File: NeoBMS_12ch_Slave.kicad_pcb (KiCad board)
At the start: 2 copper layers, 60 x 60 mm, 73 parts, among them IC1 LTC6804-2, P1 Low Cells, P2 High Cells, P3 BUS, P4 Expansion, Q1 Q_NPN_BCEC, SW1 Address, T1 CM Choke, T2 TRANSFORMER

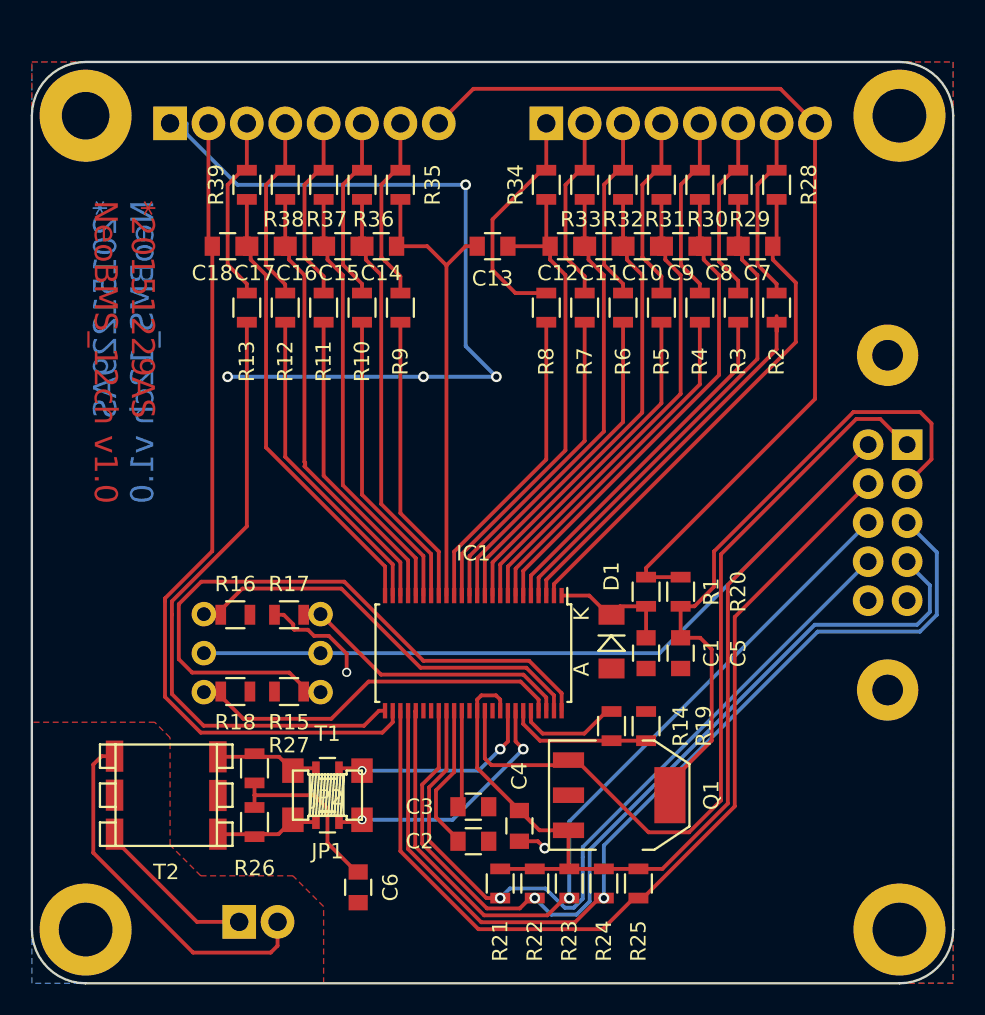
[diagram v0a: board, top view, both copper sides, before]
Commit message: - integrated balancer and filter resistors into one - changed filter/balancer resistors to 1206 - changed BIAS network to 1k5 + 470R - relocated BIAS network
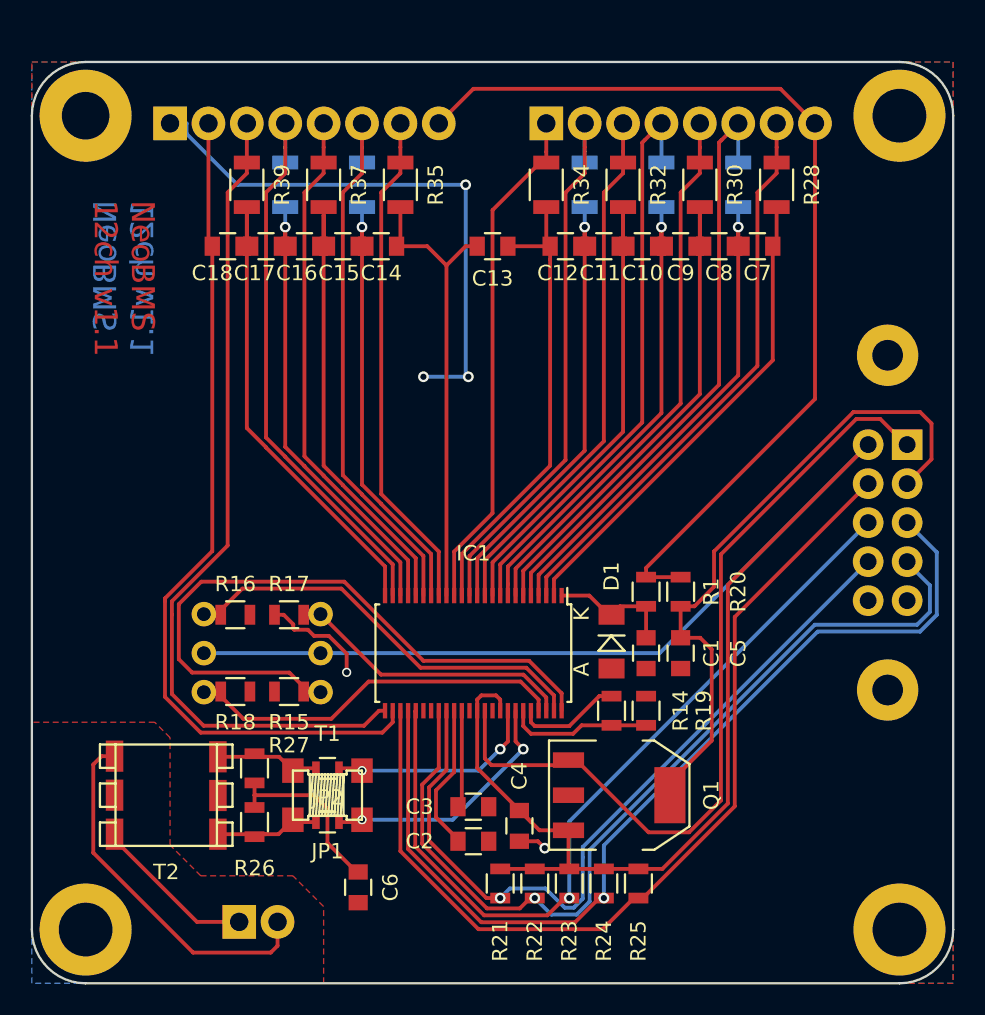
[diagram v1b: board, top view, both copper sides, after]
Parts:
- removed R10, R11, R12, R13, R2, R3, R4, R5, R6, R7, R8, R9: 100, Resistors_SMD:R_0805
- R14: value 2k7 -> 1k5
- R19: value 1k2 -> 470
- R28, R30, R32, R34, R35, R37, R39: footprint Resistors_SMD:R_0805 -> Resistors_SMD:R_1206
- R29, R31, R33, R36, R38: footprint Resistors_SMD:R_0805 -> Resistors_SMD:R_1206; moved to B.Cu
- T2: value TRANSFORMER -> PE-68386N
- moved R14 1.00 mm to (74.8, 66.2)
- moved R19 1.00 mm to (77.0, 66.2)
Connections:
- IC1 pad 11: Net-(IC1-Pad11) -> /Cell_8+
- IC1 pad 13: Net-(IC1-Pad13) -> /Cell_7+
- IC1 pad 15: Net-(IC1-Pad15) -> /Cell_6+
- IC1 pad 17: Net-(IC1-Pad17) -> /Cell_5+
- IC1 pad 19: Net-(IC1-Pad19) -> /Cell_4+
- IC1 pad 21: Net-(IC1-Pad21) -> /Cell_3+
- IC1 pad 23: Net-(IC1-Pad23) -> /Cell_2+
- IC1 pad 25: Net-(IC1-Pad25) -> /Cell_1+
- IC1 pad 3: Net-(IC1-Pad3) -> /Cell_12+
- IC1 pad 39: (no net) -> Net-(IC1-Pad39)
- IC1 pad 5: Net-(IC1-Pad5) -> /Cell_11+
- IC1 pad 7: Net-(IC1-Pad7) -> /Cell_10+
- IC1 pad 9: Net-(IC1-Pad9) -> /Cell_9+
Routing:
- net /Cell_1+: track 12.6 -> 54.3 mm
- net Net-(IC1-Pad25): track 41.4 -> 0.00 mm
- net /Cell_11+: track 12.6 -> 38.9 mm
- net /Cell_9+: track 12.6 -> 37.6 mm
- net Net-(IC1-Pad3): track 25.0 -> 0.00 mm
- net /Cell_2+: track 12.6 -> 37.2 mm
- net /Cell_12+: track 12.9 -> 37.0 mm
- net /Cell_7+: track 12.6 -> 36.4 mm
- net /Cell_4+: track 12.5 -> 36.0 mm
- net Net-(IC1-Pad5): track 23.4 -> 0.00 mm
- net /Cell_10+: track 12.6 -> 35.7 mm
- net Net-(IC1-Pad7): track 22.8 -> 0.00 mm
- net Net-(IC1-Pad9): track 22.1 -> 0.00 mm
- net /Cell_8+: track 12.5 -> 34.5 mm
- net Net-(IC1-Pad11): track 21.5 -> 0.00 mm
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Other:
- board text added: "BAT+ C12+ C11+ C10+ C9+ C8+ C7+ C6+"
- board text added: "NeoBMS 12ch v1.1"
- board text removed: "*20151229AS NeoBMS_12ch v1.0"
- board text removed: "BAT+ C12+ C11+ C1ß+ C9+ C8+ C7+ C6+"

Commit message: - jump to version 2.0 - external balancing switches
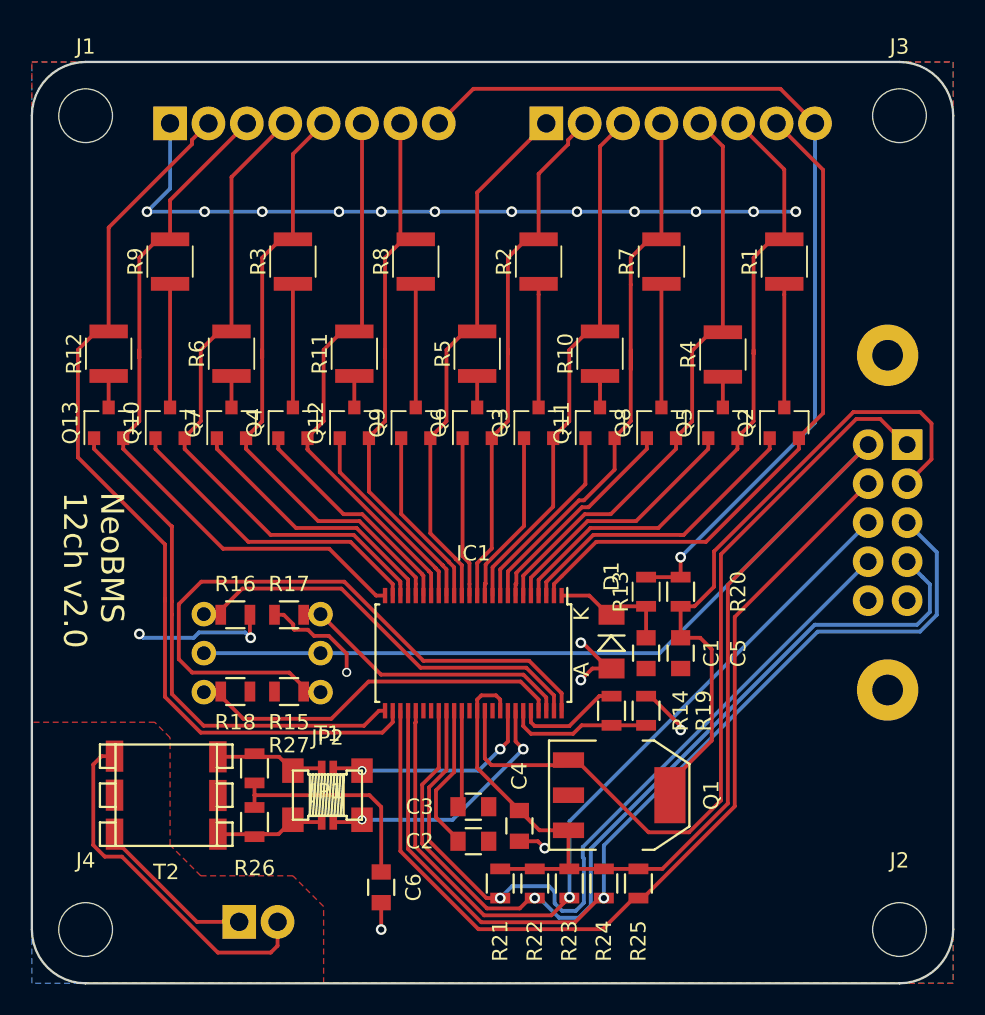
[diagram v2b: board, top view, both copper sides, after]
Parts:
- removed C10, C11, C12, C13, C14, C15, C16, C17, C18, C7, C8, C9: 100n, Capacitors_SMD:C_0805
- removed Hole_31 (x4): VAL**, alexmod:Hole_31
- removed R28, R29, R30, R31, R32, R33, R34, R35, R36, R37, R38, R39: 100, Resistors_SMD:R_1206
- added J1: Conn_01x01, Mounting_Holes:MountingHole_3.5mm, F.Cu at (40.5, 27.5)
- added J2: Conn_01x01, Mounting_Holes:MountingHole_3.5mm, F.Cu at (93.5, 80.5)
- added J3: Conn_01x01, Mounting_Holes:MountingHole_3.5mm, F.Cu at (93.5, 27.5)
- added J4: Conn_01x01, Mounting_Holes:MountingHole_3.5mm, F.Cu at (40.5, 80.5)
- added Q10: Q_PMOS_GSD, TO_SOT_Packages_SMD:SOT-23, F.Cu at (46.0, 47.5)
- added Q11: Q_PMOS_GSD, TO_SOT_Packages_SMD:SOT-23, F.Cu at (74.0, 47.5)
- added Q12: Q_PMOS_GSD, TO_SOT_Packages_SMD:SOT-23, F.Cu at (58.0, 47.5)
- added Q13: Q_PMOS_GSD, TO_SOT_Packages_SMD:SOT-23, F.Cu at (42.0, 47.5)
- added Q2: Q_PMOS_GSD, TO_SOT_Packages_SMD:SOT-23, F.Cu at (86.0, 47.5)
- added Q3: Q_PMOS_GSD, TO_SOT_Packages_SMD:SOT-23, F.Cu at (70.0, 47.5)
- added Q4: Q_PMOS_GSD, TO_SOT_Packages_SMD:SOT-23, F.Cu at (54.0, 47.5)
- added Q5: Q_PMOS_GSD, TO_SOT_Packages_SMD:SOT-23, F.Cu at (82.0, 47.5)
- added Q6: Q_PMOS_GSD, TO_SOT_Packages_SMD:SOT-23, F.Cu at (66.0, 47.5)
- added Q7: Q_PMOS_GSD, TO_SOT_Packages_SMD:SOT-23, F.Cu at (50.0, 47.5)
- added Q8: Q_PMOS_GSD, TO_SOT_Packages_SMD:SOT-23, F.Cu at (78.0, 47.5)
- added Q9: Q_PMOS_GSD, TO_SOT_Packages_SMD:SOT-23, F.Cu at (62.0, 47.5)
- added R10: 33R, Resistors_SMD:R_1210, F.Cu at (74.0, 43.0)
- added R11: 33R, Resistors_SMD:R_1210, F.Cu at (58.0, 43.0)
- added R12: 33R, Resistors_SMD:R_1210, F.Cu at (42.0, 43.0)
- added R13: 100R, Resistors_SMD:R_0805, F.Cu at (77.0, 58.5)
- added R2: 33R, Resistors_SMD:R_1210, F.Cu at (70.0, 37.0)
- added R3: 33R, Resistors_SMD:R_1210, F.Cu at (54.0, 37.0)
- added R4: 33R, Resistors_SMD:R_1210, F.Cu at (82.0, 43.1)
- added R5: 33R, Resistors_SMD:R_1210, F.Cu at (66.0, 43.0)
- added R6: 33R, Resistors_SMD:R_1210, F.Cu at (50.0, 43.0)
- added R7: 33R, Resistors_SMD:R_1210, F.Cu at (78.0, 37.0)
- added R8: 33R, Resistors_SMD:R_1210, F.Cu at (62.0, 37.0)
- added R9: 33R, Resistors_SMD:R_1210, F.Cu at (46.0, 37.0)
- JP1, JP2: footprint Resistors_SMD:R_0603 -> alexmod:Jumper_2
- R1: value 100 -> 33R; footprint Resistors_SMD:R_0805 -> Resistors_SMD:R_1210
- moved R1 23.3 mm to (86.0, 37.0), turned to 90 degrees
- moved C6 1.50 mm to (59.8, 77.8)
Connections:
- net /Cell1- renamed /Cell_1-
- IC1 pad 10: Net-(C10-Pad2) -> /Cell_8+
- IC1 pad 11: /Cell_8+ -> Net-(IC1-Pad11)
- IC1 pad 12: Net-(C11-Pad2) -> /Cell_7+
- IC1 pad 13: /Cell_7+ -> Net-(IC1-Pad13)
- IC1 pad 14: Net-(C12-Pad2) -> /Cell_6+
- IC1 pad 15: /Cell_6+ -> Net-(IC1-Pad15)
- IC1 pad 16: Net-(C13-Pad2) -> /Cell_5+
- IC1 pad 17: /Cell_5+ -> Net-(IC1-Pad17)
- IC1 pad 18: Net-(C14-Pad2) -> /Cell_4+
- IC1 pad 19: /Cell_4+ -> Net-(IC1-Pad19)
- IC1 pad 2: Net-(C7-Pad1) -> /Cell_12+
- IC1 pad 20: Net-(C15-Pad2) -> /Cell_3+
- IC1 pad 21: /Cell_3+ -> Net-(IC1-Pad21)
- IC1 pad 22: Net-(C16-Pad2) -> /Cell_2+
- IC1 pad 23: /Cell_2+ -> Net-(IC1-Pad23)
- IC1 pad 24: Net-(C17-Pad2) -> /Cell_1+
- IC1 pad 25: /Cell_1+ -> Net-(IC1-Pad25)
- IC1 pad 3: /Cell_12+ -> Net-(IC1-Pad3)
- IC1 pad 39: Net-(IC1-Pad39) -> (no net)
- IC1 pad 4: Net-(C7-Pad2) -> /Cell_11+
- IC1 pad 5: /Cell_11+ -> Net-(IC1-Pad5)
- IC1 pad 6: Net-(C8-Pad2) -> /Cell_10+
- IC1 pad 7: /Cell_10+ -> Net-(IC1-Pad7)
- IC1 pad 8: Net-(C10-Pad1) -> /Cell_9+
- IC1 pad 9: /Cell_9+ -> Net-(IC1-Pad9)
- R1 pad 1: /BAT+ -> Net-(Q2-Pad3)
- R1 pad 2: Net-(C1-Pad1) -> /Cell_11+
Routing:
- net Net-(IC1-Pad25): track 0.00 -> 33.9 mm
- net Net-(C8-Pad2): track 33.2 -> 0.00 mm
- net Net-(C7-Pad2): track 32.5 -> 0.00 mm, vias 1 -> 0
- net Net-(C10-Pad2): track 32.0 -> 0.00 mm
- net Net-(C17-Pad2): track 31.7 -> 0.00 mm
- net Net-(C7-Pad1): track 31.3 -> 0.00 mm
- net Net-(C10-Pad1): track 31.3 -> 0.00 mm, vias 1 -> 0
- net GND: track 45.8 -> 76.8 mm, vias 5 -> 20
- net Net-(C12-Pad2): track 30.5 -> 0.00 mm
- net Net-(C13-Pad2): track 30.4 -> 0.00 mm
- net Net-(C11-Pad2): track 30.1 -> 0.00 mm, vias 1 -> 0
- net Net-(C15-Pad2): track 29.9 -> 0.00 mm
- net Net-(C16-Pad2): track 29.8 -> 0.00 mm, vias 1 -> 0
- net Net-(C14-Pad2): track 28.5 -> 0.00 mm, vias 1 -> 0
- net Net-(IC1-Pad23): track 0.00 -> 20.5 mm
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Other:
- rule pad_to_mask_clearance: 0.2 -> 0.1
- board text added: "B+ 12+ 11+ 10+ 9+ 8+ 7+ 6+"
- board text added: "B+ 5+ 4+ 3+ 2+ 1+ 1- B-"
- board text added: "NeoBMS 12ch v2.0"
- board text removed: "BAT+ C12+ C11+ C10+ C9+ C8+ C7+ C6+"
- board text removed: "BAT+ C5+ C4+ C3+ C2+ C1+ C1- BAT-"
- board text removed: "NeoBMS 12ch v1.1"
